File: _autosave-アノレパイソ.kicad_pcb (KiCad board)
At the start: 2 copper layers, 178 x 50 mm, 29 parts, among them SW0 RotaryEncoder_Switch, SW1 SW_PUSH, SW2 SW_PUSH, SW3 SW_PUSH, SW4 SW_PUSH, SW5 SW_PUSH, SW6 SW_PUSH, SW9 SW_PUSH, U1 SO1602AWWB-UC-WB-U, U3 ProMicro

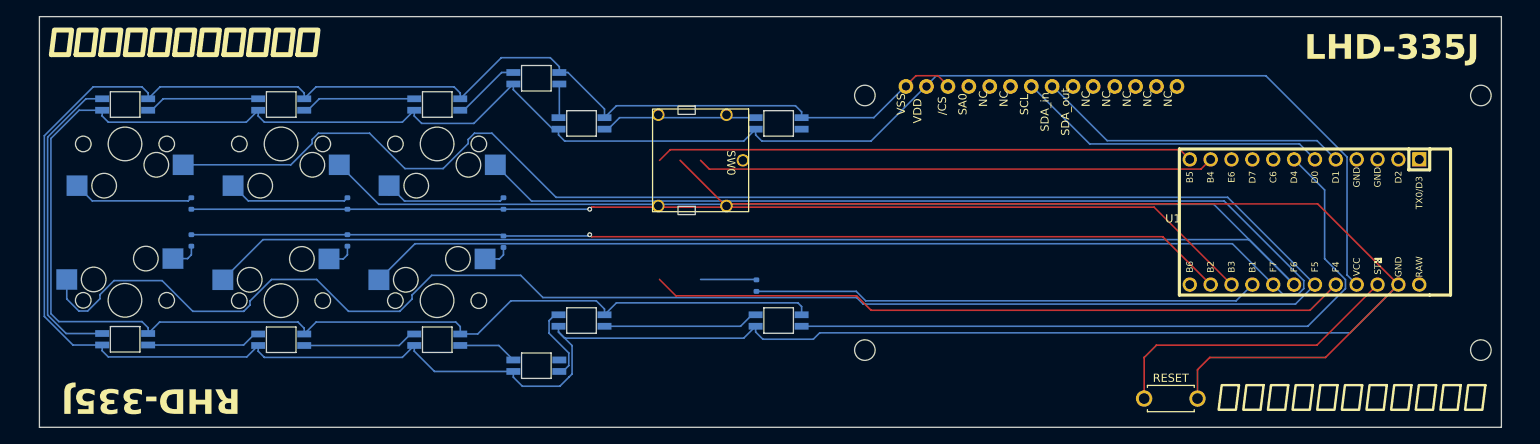
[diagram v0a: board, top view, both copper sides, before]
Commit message: 2/5(水)定例MTG指摘対策版
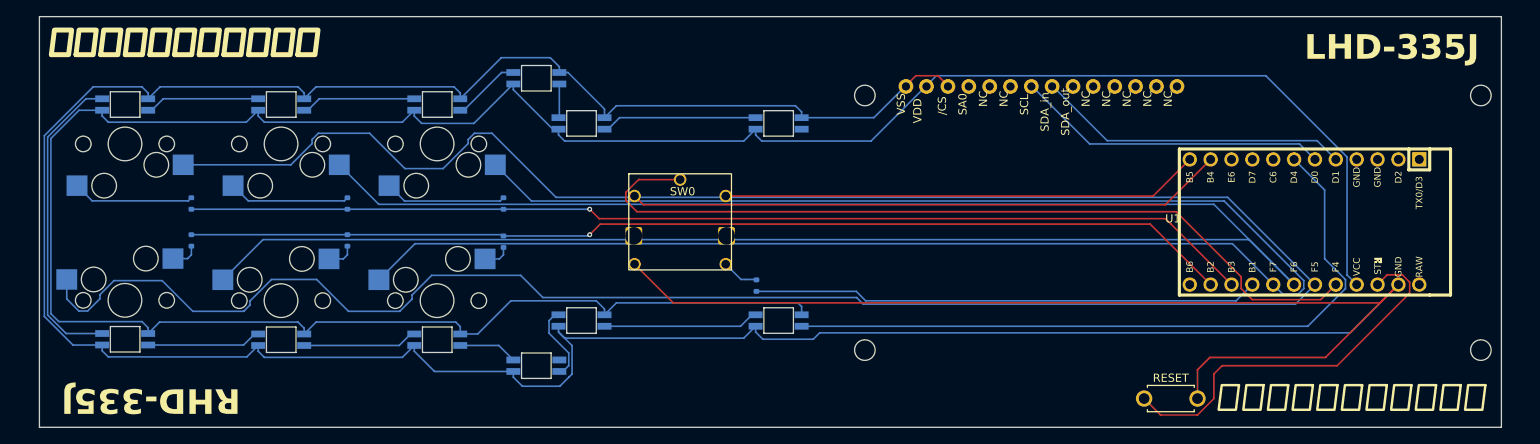
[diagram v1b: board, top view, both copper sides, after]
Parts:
- moved SW0 7.89 mm to (124.0, 75.0), turned to 0 degrees
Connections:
- SW0 pad S1: (no net) -> Net-(D0-A)
- SW0 pad S2: (no net) -> Col0
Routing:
- net Col0: track 85.2 -> 101.3 mm
- net Reset: track 37.1 -> 47.2 mm
- net RE_A: track 63.0 -> 72.9 mm
- net RE_B: track 65.6 -> 58.5 mm
- net Net-(D0-A): track 6.82 -> 4.53 mm
- net GND: track 460.9 -> 463.0 mm
- net Row2: track 126.7 -> 127.8 mm
